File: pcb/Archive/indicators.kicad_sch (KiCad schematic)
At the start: 4 parts

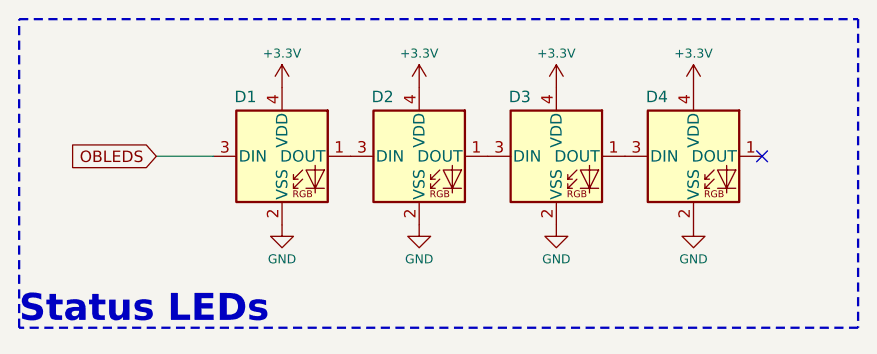
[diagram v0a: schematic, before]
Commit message: Added interfaces and fully routed PCB
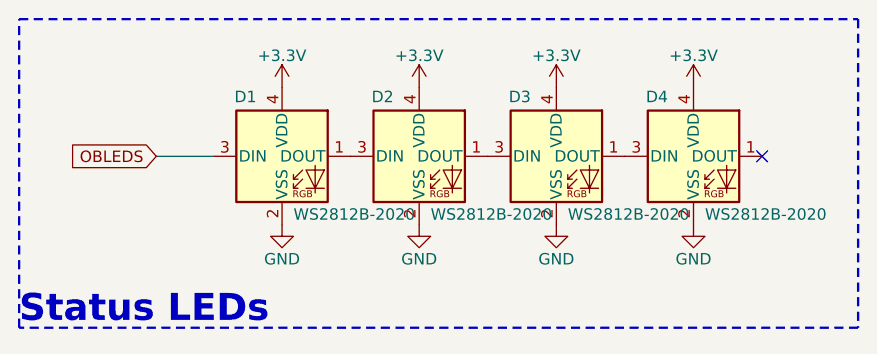
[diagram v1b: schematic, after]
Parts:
- D1, D2, D3, D4: LCSC C2976072 -> (none); MN World Semi -> (none); MPN WS2812C-2020-V1 -> (none)
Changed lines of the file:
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@@
 		)
 		(property "Value" "WS2812B-2020"
-			(at 75.692 27.178 0)
-			(effects
-				(font
-					(size 1.27 1.27)
-				)
-				(hide yes)
+			(at 86.36 40.005 0)
+			(effects
+				(font
+					(size 1.27 1.27)
+				)
+				(justify left top)
 			)
 		)
@@
 			)
 		)
-		(property "MN" "World Semi"
-			(at 85.09 34.29 0)
-			(effects
-				(font
-					(size 1.27 1.27)
-				)
-				(hide yes)
-			)
-		)
-		(property "MPN" "WS2812C-2020-V1"
-			(at 85.09 34.29 0)
-			(effects
-				(font
-					(size 1.27 1.27)
-				)
-				(hide yes)
-			)
-		)
-		(property "Digikey" ""
-			(at 85.09 34.29 0)
-			(effects
-				(font
-					(size 1.27 1.27)
-				)
-				(hide yes)
-			)
-		)
-		(property "Mouser" ""
-			(at 85.09 34.29 0)
-			(effects
-				(font
-					(size 1.27 1.27)
-				)
-				(hide yes)
-			)
-		)
-		(property "LCSC" "C2976072"
-			(at 85.09 34.29 0)
-			(effects
-				(font
-					(size 1.27 1.27)
-				)
-				(hide yes)
-			)
-		)
 		(pin "4"
 		)
@@
 		)
 		(property "Value" "+3.3V"
-			(at 54.61 22.86 0)
-			(effects
-				(font
-					(size 1 1)
+			(at 54.61 23.114 0)
+			(effects
+				(font
+					(size 1.27 1.27)
 				)
 			)
@@
 			(effects
 				(font
-					(size 1 1)
-					(color 223 129 255 1)
+					(size 1.27 1.27)
 				)
 				(hide yes)
@@
 			(effects
 				(font
-					(size 1 1)
-					(color 223 129 255 1)
+					(size 1.27 1.27)
 				)
 				(hide yes)
@@
 		)
 		(property "Value" "WS2812B-2020"
-			(at 60.452 27.178 0)
-			(effects
-				(font
-					(size 1.27 1.27)
-				)
-				(hide yes)
+			(at 71.12 40.005 0)
+			(effects
+				(font
+					(size 1.27 1.27)
+				)
+				(justify left top)
 			)
 		)
@@
 			)
 		)
-		(property "MN" "World Semi"
-			(at 69.85 34.29 0)
-			(effects
-				(font
-					(size 1.27 1.27)
-				)
-				(hide yes)
-			)
-		)
-		(property "MPN" "WS2812C-2020-V1"
-			(at 69.85 34.29 0)
-			(effects
-				(font
-					(size 1.27 1.27)
-				)
-				(hide yes)
-			)
-		)
-		(property "Digikey" ""
-			(at 69.85 34.29 0)
-			(effects
-				(font
-					(size 1.27 1.27)
-				)
-				(hide yes)
-			)
-		)
-		(property "Mouser" ""
-			(at 69.85 34.29 0)
-			(effects
-				(font
-					(size 1.27 1.27)
-				)
-				(hide yes)
-			)
-		)
-		(property "LCSC" "C2976072"
-			(at 69.85 34.29 0)
-			(effects
-				(font
-					(size 1.27 1.27)
-				)
-				(hide yes)
-			)
-		)
 		(pin "4"
 		)
@@
 			(effects
 				(font
-					(size 1 1)
+					(size 1.27 1.27)
 				)
 			)
@@
 			(effects
 				(font
-					(size 1 1)
-					(color 223 129 255 1)
+					(size 1.27 1.27)
 				)
 				(hide yes)
@@
 			(effects
 				(font
-					(size 1 1)
-					(color 223 129 255 1)
+					(size 1.27 1.27)
 				)
 				(hide yes)
@@
 			(effects
 				(font
-					(size 1 1)
+					(size 1.27 1.27)
 				)
 			)
@@
 			(effects
 				(font
-					(size 1 1)
-					(color 223 129 255 1)
+					(size 1.27 1.27)
 				)
 				(hide yes)
@@
 			(effects
 				(font
-					(size 1 1)
-					(color 223 129 255 1)
+					(size 1.27 1.27)
 				)
 				(hide yes)
@@
 		)
 		(property "Value" "+3.3V"
-			(at 85.09 22.86 0)
-			(effects
-				(font
-					(size 1 1)
+			(at 85.09 23.114 0)
+			(effects
+				(font
+					(size 1.27 1.27)
 				)
 			)
@@
 			(effects
 				(font
-					(size 1 1)
-					(color 223 129 255 1)
+					(size 1.27 1.27)
 				)
 				(hide yes)
@@
 			(effects
 				(font
-					(size 1 1)
-					(color 223 129 255 1)
+					(size 1.27 1.27)
 				)
 				(hide yes)
@@
 		)
 		(property "Value" "WS2812B-2020"
-			(at 45.212 27.178 0)
-			(effects
-				(font
-					(size 1.27 1.27)
-				)
-				(hide yes)
+			(at 55.88 40.005 0)
+			(effects
+				(font
+					(size 1.27 1.27)
+				)
+				(justify left top)
 			)
 		)
@@
 			)
 		)
-		(property "MN" "World Semi"
-			(at 54.61 34.29 0)
-			(effects
-				(font
-					(size 1.27 1.27)
-				)
-				(hide yes)
-			)
-		)
-		(property "MPN" "WS2812C-2020-V1"
-			(at 54.61 34.29 0)
-			(effects
-				(font
-					(size 1.27 1.27)
-				)
-				(hide yes)
-			)
-		)
-		(property "Digikey" ""
-			(at 54.61 34.29 0)
-			(effects
-				(font
-					(size 1.27 1.27)
-				)
-				(hide yes)
-			)
-		)
-		(property "Mouser" ""
-			(at 54.61 34.29 0)
-			(effects
-				(font
-					(size 1.27 1.27)
-				)
-				(hide yes)
-			)
-		)
-		(property "LCSC" "C2976072"
-			(at 54.61 34.29 0)
-			(effects
-				(font
-					(size 1.27 1.27)
-				)
-				(hide yes)
-			)
-		)
 		(pin "4"
 		)
@@
 		)
 		(property "Value" "WS2812B-2020"
-			(at 90.932 27.178 0)
-			(effects
-				(font
-					(size 1.27 1.27)
-				)
-				(hide yes)
+			(at 101.6 40.005 0)
+			(effects
+				(font
+					(size 1.27 1.27)
+				)
+				(justify left top)
 			)
 		)
@@
 			)
 		)
-		(property "MN" "World Semi"
-			(at 100.33 34.29 0)
-			(effects
-				(font
-					(size 1.27 1.27)
-				)
-				(hide yes)
-			)
-		)
-		(property "MPN" "WS2812C-2020-V1"
-			(at 100.33 34.29 0)
-			(effects
-				(font
-					(size 1.27 1.27)
-				)
-				(hide yes)
-			)
-		)
-		(property "Digikey" ""
-			(at 100.33 34.29 0)
-			(effects
-				(font
-					(size 1.27 1.27)
-				)
-				(hide yes)
-			)
-		)
-		(property "Mouser" ""
-			(at 100.33 34.29 0)
-			(effects
-				(font
-					(size 1.27 1.27)
-				)
-				(hide yes)
-			)
-		)
-		(property "LCSC" "C2976072"
-			(at 100.33 34.29 0)
-			(effects
-				(font
-					(size 1.27 1.27)
-				)
-				(hide yes)
-			)
-		)
 		(pin "4"
 		)
@@
 			(effects
 				(font
-					(size 1 1)
+					(size 1.27 1.27)
 				)
 			)
@@
 			(effects
 				(font
-					(size 1 1)
-					(color 223 129 255 1)
+					(size 1.27 1.27)
 				)
 				(hide yes)
@@
 			(effects
 				(font
-					(size 1 1)
-					(color 223 129 255 1)
+					(size 1.27 1.27)
 				)
 				(hide yes)
@@
 			(effects
 				(font
-					(size 1 1)
+					(size 1.27 1.27)
 				)
 			)
@@
 			(effects
 				(font
-					(size 1 1)
-					(color 223 129 255 1)
+					(size 1.27 1.27)
 				)
 				(hide yes)
@@
 			(effects
 				(font
-					(size 1 1)
-					(color 223 129 255 1)
+					(size 1.27 1.27)
 				)
 				(hide yes)
@@
 		)
 		(property "Value" "+3.3V"
-			(at 69.85 22.86 0)
-			(effects
-				(font
-					(size 1 1)
+			(at 69.85 23.114 0)
+			(effects
+				(font
+					(size 1.27 1.27)
 				)
 			)
@@
 			(effects
 				(font
-					(size 1 1)
-					(color 223 129 255 1)
+					(size 1.27 1.27)
 				)
 				(hide yes)
@@
 			(effects
 				(font
-					(size 1 1)
-					(color 223 129 255 1)
+					(size 1.27 1.27)
 				)
 				(hide yes)
@@
 		)
 		(property "Value" "+3.3V"
-			(at 100.33 22.86 0)
-			(effects
-				(font
-					(size 1 1)
+			(at 100.33 23.114 0)
+			(effects
+				(font
+					(size 1.27 1.27)
 				)
 			)
@@
 			(effects
 				(font
-					(size 1 1)
-					(color 223 129 255 1)
+					(size 1.27 1.27)
 				)
 				(hide yes)
@@
 			(effects
 				(font
-					(size 1 1)
-					(color 223 129 255 1)
-				)
-				(hide yes)
+					(size 1.27 1.27)
+				)
+				(hide yes)
